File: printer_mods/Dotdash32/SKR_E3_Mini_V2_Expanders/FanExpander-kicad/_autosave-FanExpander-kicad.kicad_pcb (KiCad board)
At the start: 2 copper layers, 46.3 x 37.3 mm, 69 parts, among them J0 FAN0, J1 FAN1, J10 FAN0_IN, J12 HI_PWR_IN, J2 FAN2, J3 FAN3, J4 FAN4, J5 FAN5, J6 FAN6, J7 FAN7, J8 EXP1_IN, J9 5V_In, Q1 IRLML6344, Q2 IRLML6344, Q3 IRLML6344, Q4 IRLML6344, Q5 IRLML6344, Q6 IRLML6344, Q7 IRLML6344

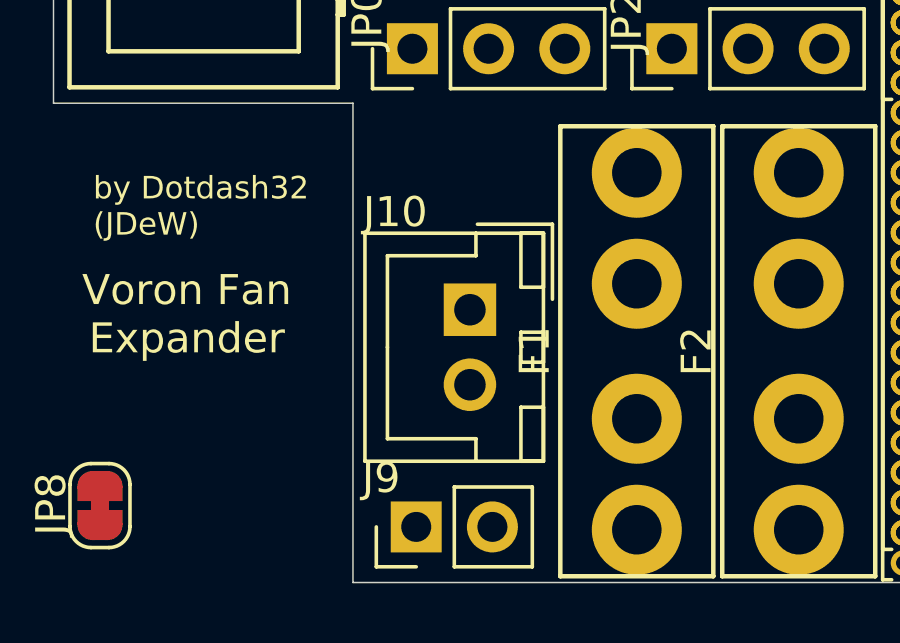
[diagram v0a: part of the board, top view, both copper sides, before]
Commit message: test: move to ATM fuses, keep breakaway
I don't think the breakaway is actuall worthwhile??
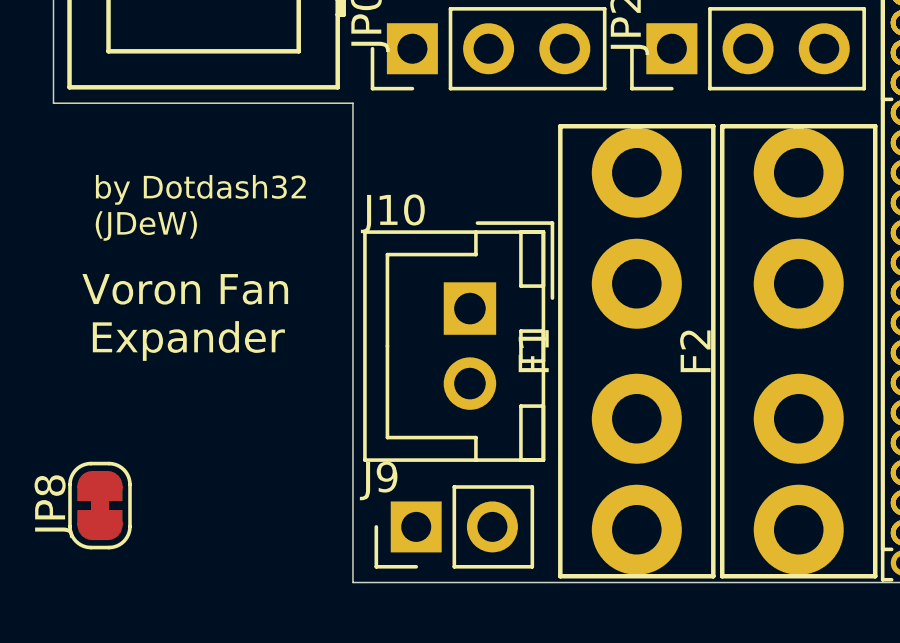
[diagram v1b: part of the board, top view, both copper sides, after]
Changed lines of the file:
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@@
   )
   (module Connectors_JST:JST_XH_B02B-XH-A_02x2.50mm_Straight (layer F.Cu)
-    (at 50.4317 74.803 270)
+    (at 50.4317 74.7649 270)
     (descr "JST XH series connector, B02B-XH-A, top entry type, through hole")
     (tags "connector jst xh tht top vertical 2.50mm")
